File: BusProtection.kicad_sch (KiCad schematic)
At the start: 90 parts, among them Q1 NX3008NBKS, Q10 MBT2222ADW1T1, Q11 NX3008NBKS, Q12 MBT2222ADW1T1, Q13 NX3008NBKS, Q14 MBT2222ADW1T1, Q15 NX3008NBKS, Q16 MBT2222ADW1T1, Q17 MMBT2907, Q18 MMBT2907, Q19 MMBT2907, Q2 MBT2222ADW1T1, Q3 NX3008NBKS, Q4 MBT2222ADW1T1, Q5 NX3008NBKS, Q6 MBT2222ADW1T1, Q7 NX3008NBKS, Q8 MBT2222ADW1T1, Q9 NX3008NBKS

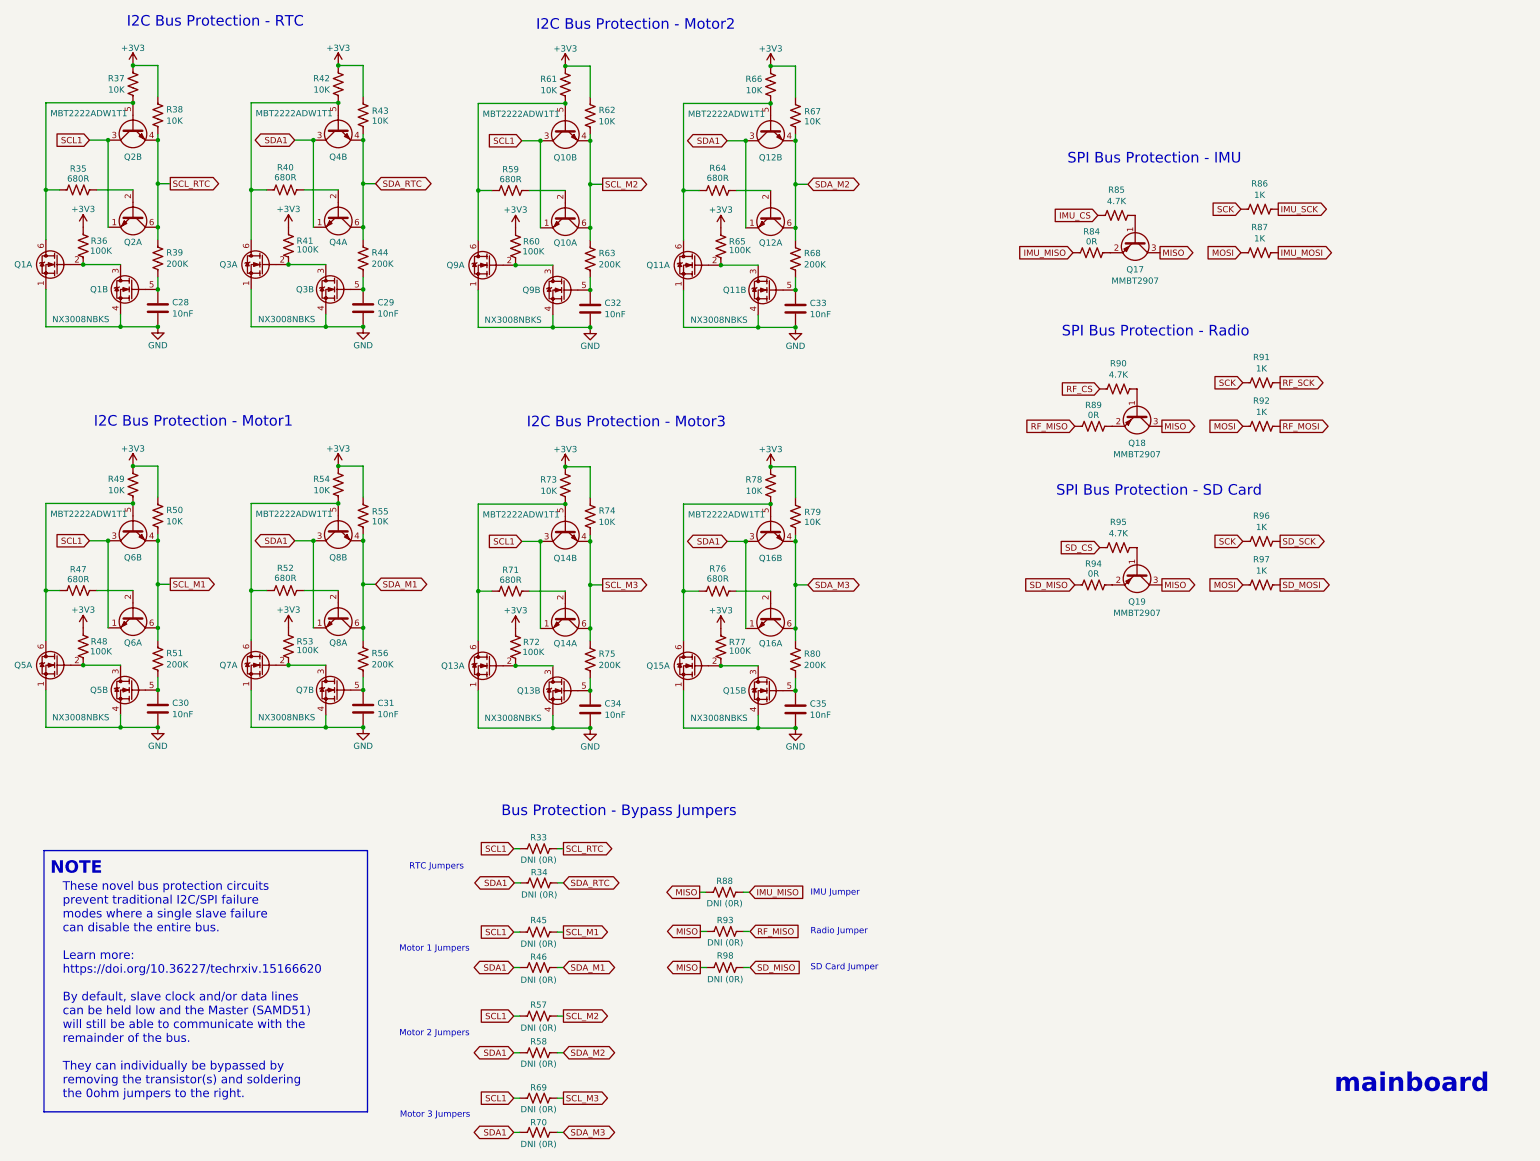
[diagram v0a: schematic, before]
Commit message: Re-wired IMU to use UART
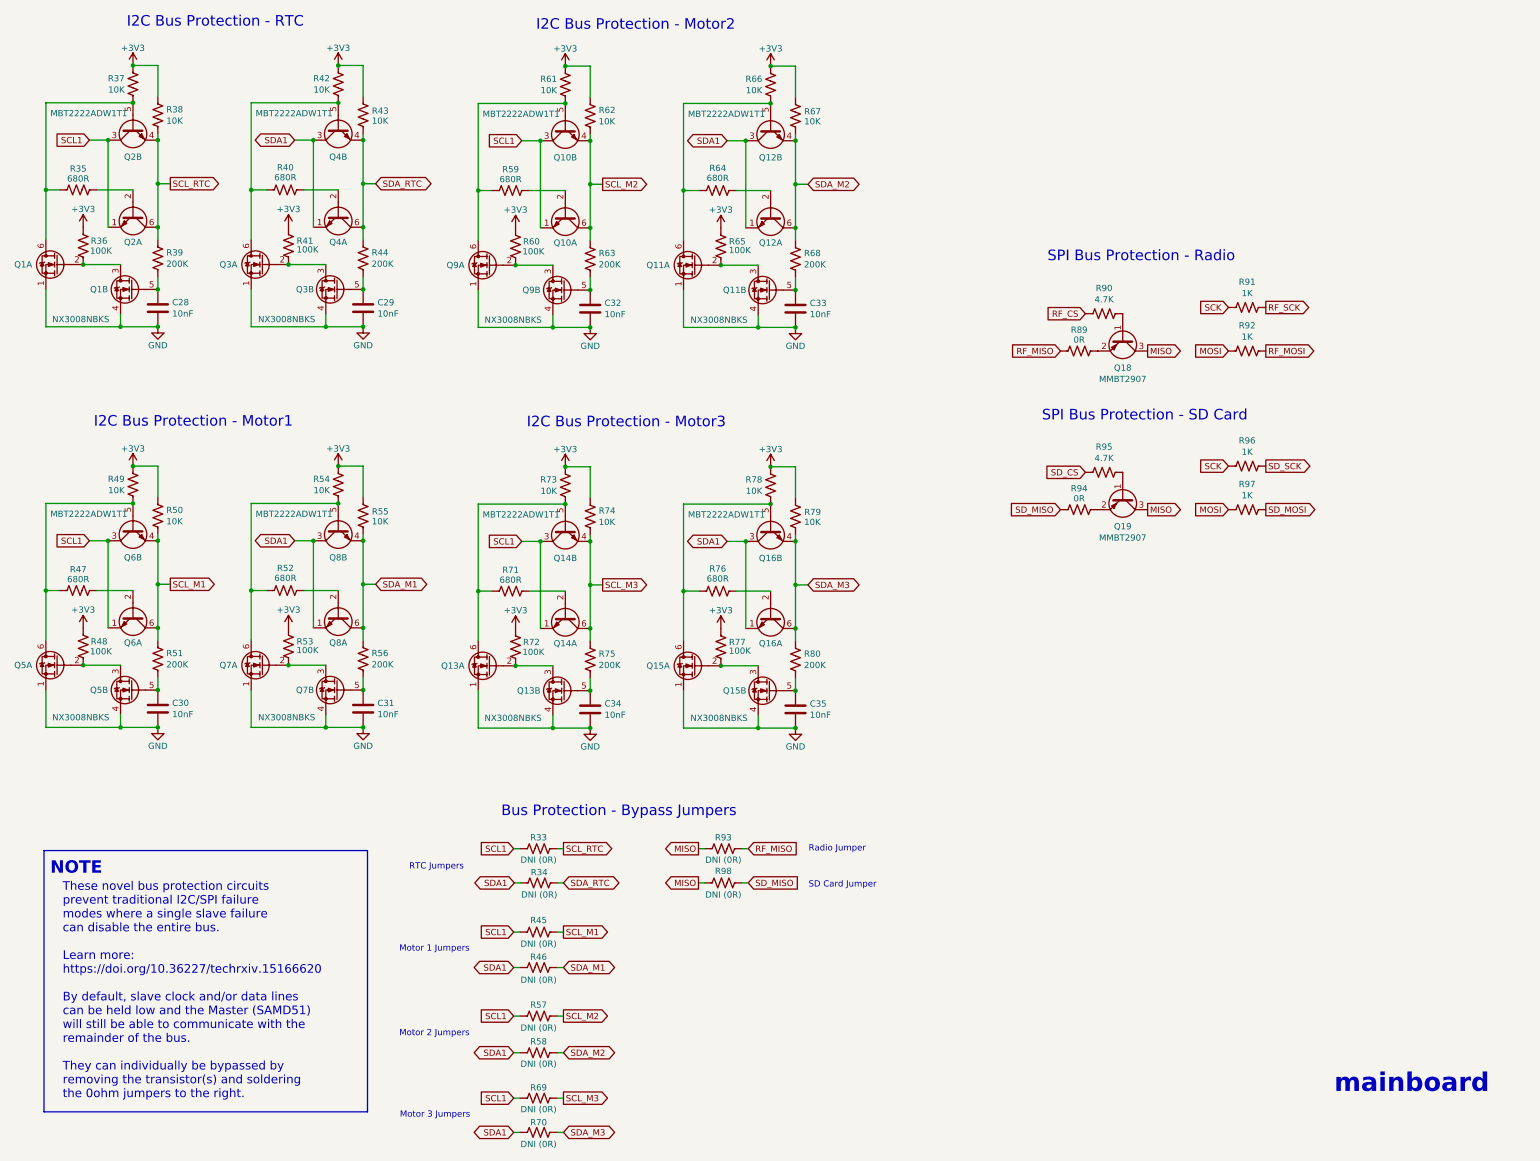
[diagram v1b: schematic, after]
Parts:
- removed Q17: MMBT2907, Package_TO_SOT_SMD:SOT-23, symbol mainboard:MMBT2907
- removed R84: 0R, Resistor_SMD:R_0603_1608Metric, symbol Device:R_US
- removed R85: 4.7K, Resistor_SMD:R_0603_1608Metric, symbol Device:R_US
- removed R86, R87: 1K, Resistor_SMD:R_0603_1608Metric, symbol Device:R_US
- removed R88: DNI (0R), Resistor_SMD:R_0603_1608Metric, symbol Device:R_US
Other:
- note removed: "IMU Jumper"
- note removed: "SPI Bus Protection - IMU"
- moved on the sheet: Q18, Q19, R89, R90, R91, R92, R93, R94, R95, R96, R97, R98

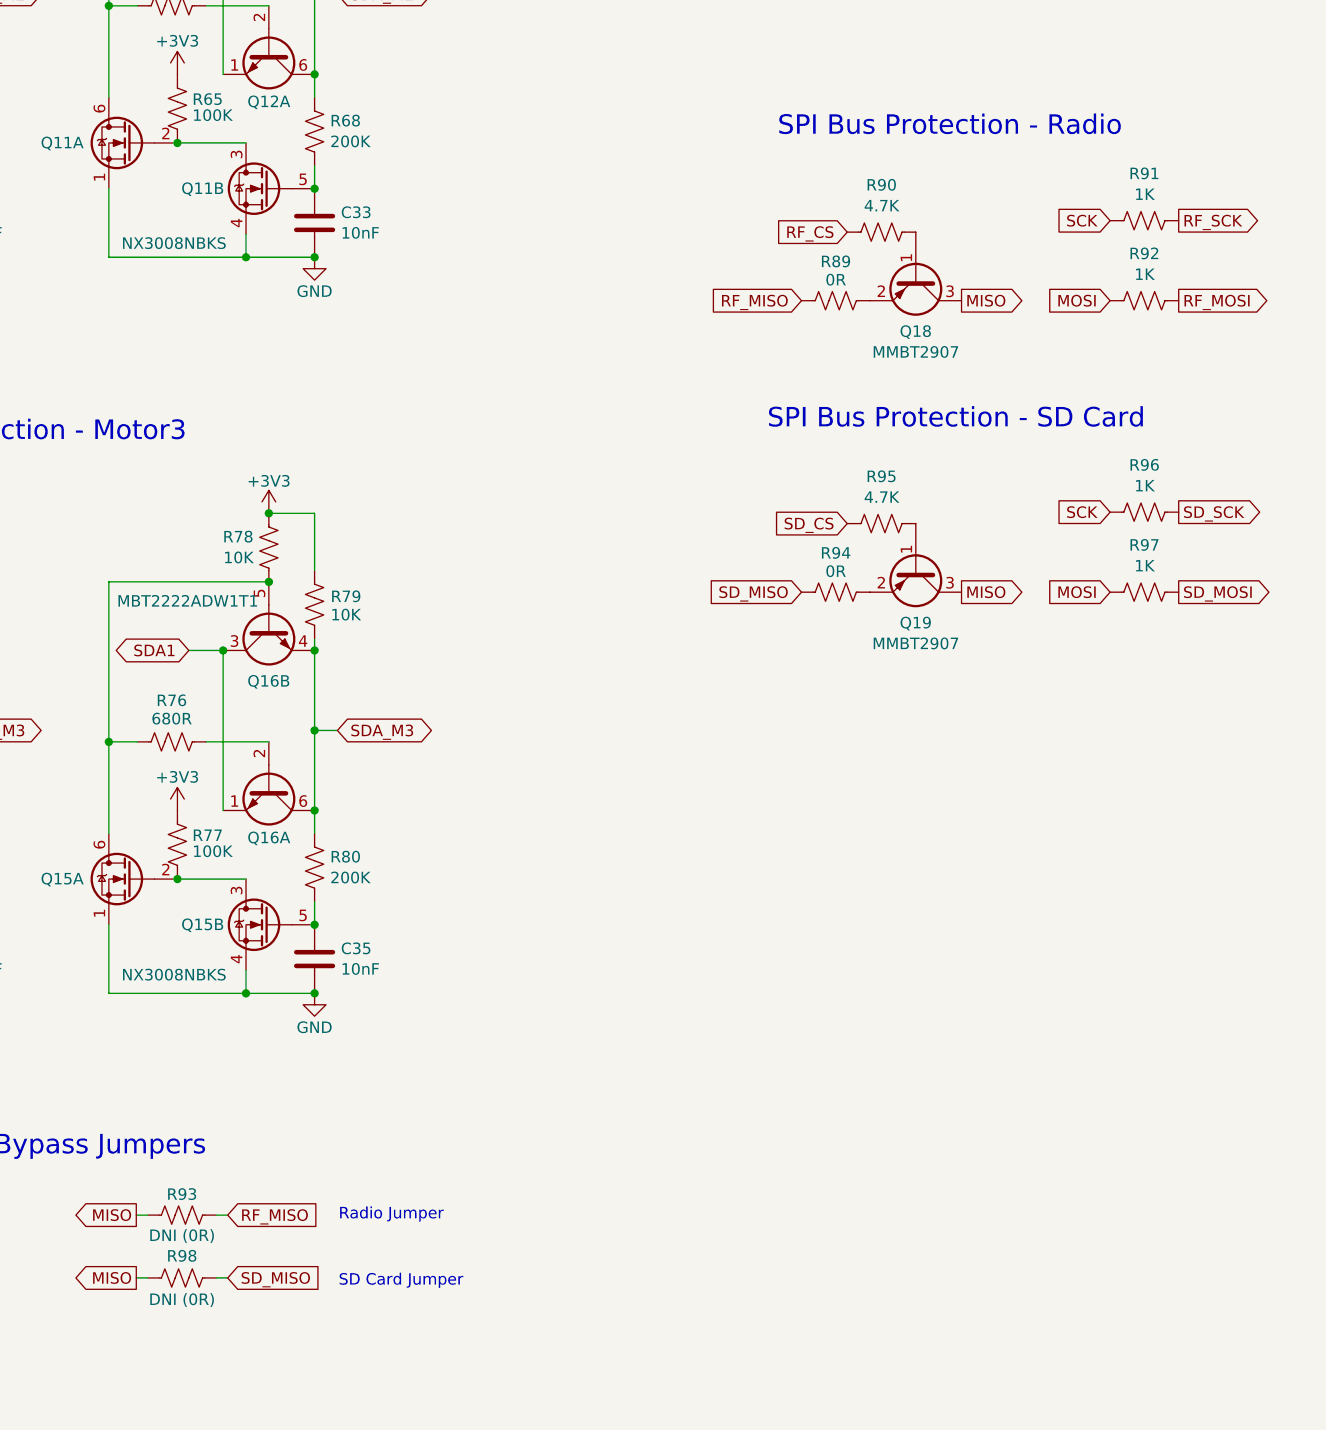
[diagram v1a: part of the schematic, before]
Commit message: Moved Rev label to be visible post-assembly
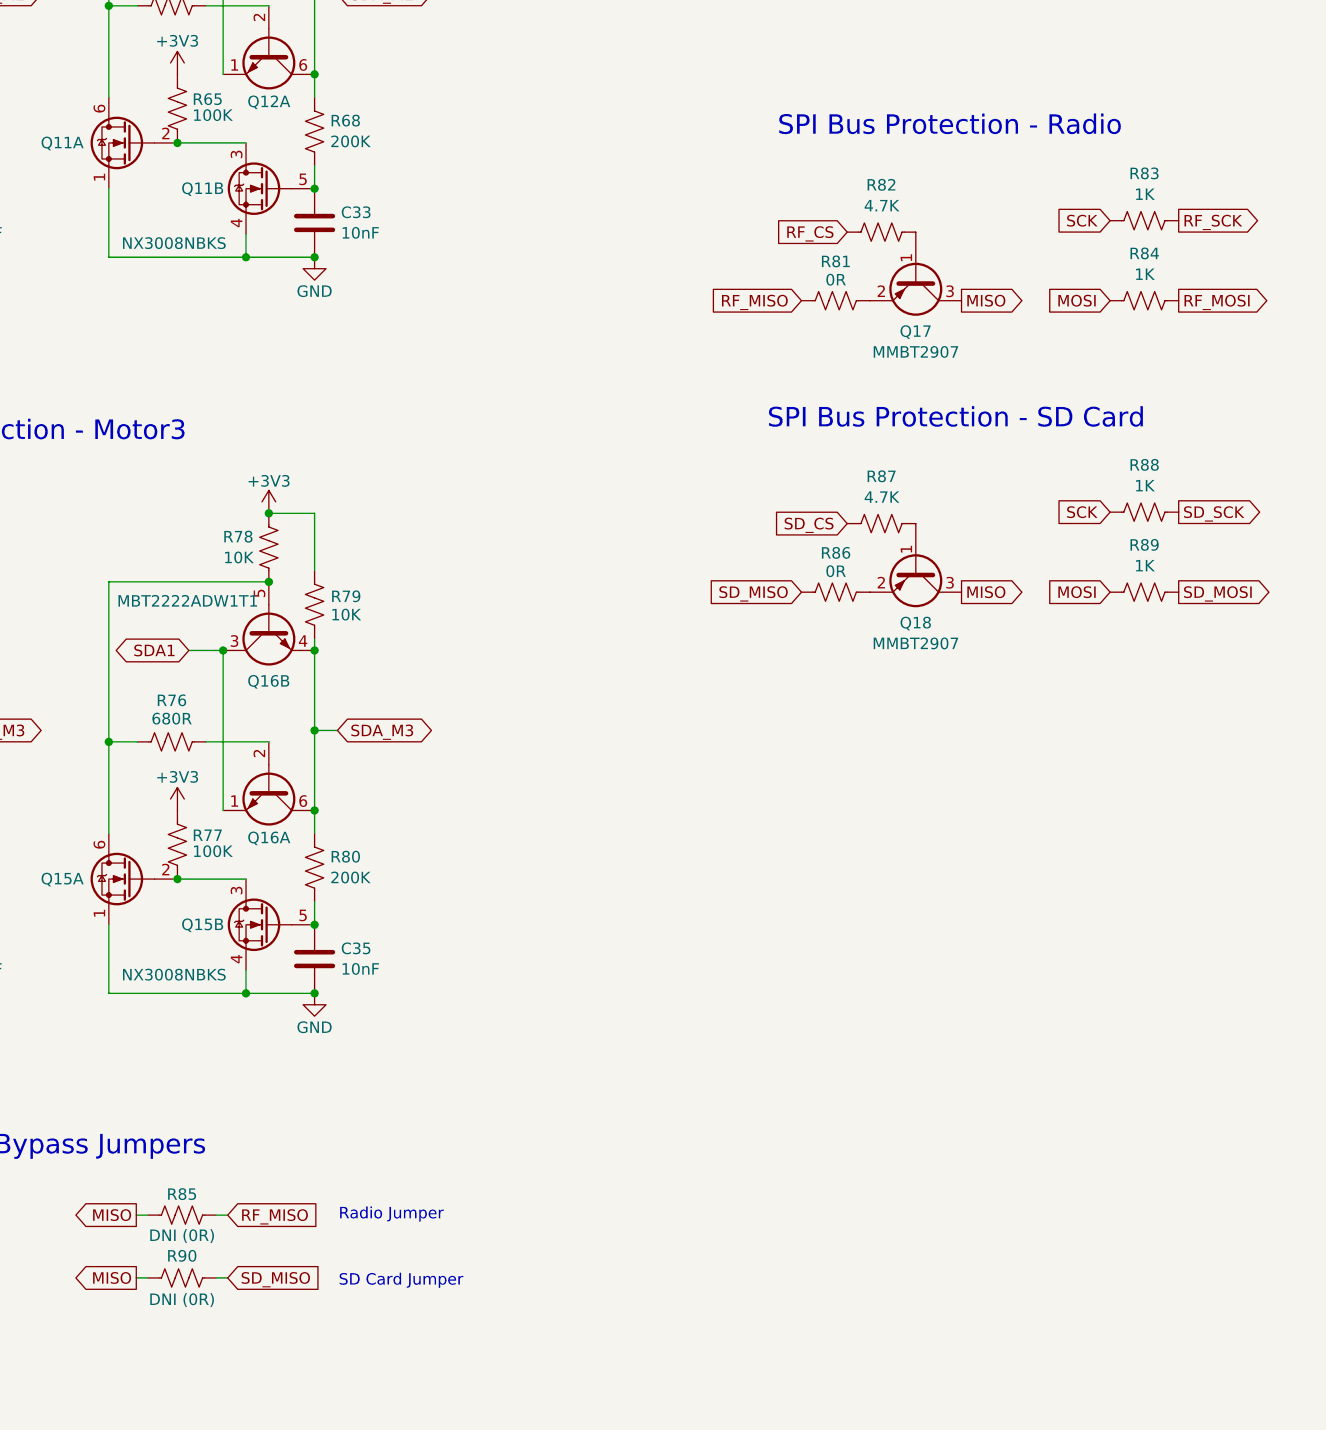
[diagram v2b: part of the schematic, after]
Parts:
- renumbered Q18 to Q17, Q19 to Q18, R89 to R81, R90 to R82, R91 to R83, R92 to R84, R93 to R85, R94 to R86, R95 to R87, R96 to R88, R97 to R89, R98 to R90
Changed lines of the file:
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@@
   (symbol (lib_id "Device:R_US") (at 298.323 126.492 270) (unit 1)
     (in_bom yes) (on_board yes) (dnp no)
-    (property "Reference" "R94" (at 298.323 122.174 90)
+    (property "Reference" "R86" (at 298.323 122.174 90)
       (effects (font (size 1.27 1.27)))
     )
@@
       (project "mainboard"
         (path "/1aa2047c-1463-47dc-8fa9-594d0cbf3c24/89e9ad27-deb2-49f4-bcf8-1a7a63ce9e3a"
-          (reference "R94") (unit 1)
+          (reference "R86") (unit 1)
         )
       )
@@
   (symbol (lib_id "Device:R_US") (at 225.679 202.692 270) (unit 1)
     (in_bom yes) (on_board yes) (dnp no)
-    (property "Reference" "R98" (at 225.679 200.279 90)
+    (property "Reference" "R90" (at 225.679 200.279 90)
       (effects (font (size 1.27 1.27)))
     )
@@
       (project "mainboard"
         (path "/1aa2047c-1463-47dc-8fa9-594d0cbf3c24/89e9ad27-deb2-49f4-bcf8-1a7a63ce9e3a"
-          (reference "R98") (unit 1)
+          (reference "R90") (unit 1)
         )
       )
@@
   (symbol (lib_id "Device:R_US") (at 332.613 94.107 270) (unit 1)
     (in_bom yes) (on_board yes) (dnp no)
-    (property "Reference" "R92" (at 332.613 88.9 90)
+    (property "Reference" "R84" (at 332.613 88.9 90)
       (effects (font (size 1.27 1.27)))
     )
@@
       (project "mainboard"
         (path "/1aa2047c-1463-47dc-8fa9-594d0cbf3c24/89e9ad27-deb2-49f4-bcf8-1a7a63ce9e3a"
-          (reference "R92") (unit 1)
+          (reference "R84") (unit 1)
         )
       )
@@
   (symbol (lib_id "Device:R_US") (at 332.613 126.492 270) (unit 1)
     (in_bom yes) (on_board yes) (dnp no)
-    (property "Reference" "R97" (at 332.613 121.285 90)
+    (property "Reference" "R89" (at 332.613 121.285 90)
       (effects (font (size 1.27 1.27)))
     )
@@
       (project "mainboard"
         (path "/1aa2047c-1463-47dc-8fa9-594d0cbf3c24/89e9ad27-deb2-49f4-bcf8-1a7a63ce9e3a"
-          (reference "R97") (unit 1)
+          (reference "R89") (unit 1)
         )
       )
@@
   (symbol (lib_id "Device:R_US") (at 303.403 118.872 270) (unit 1)
     (in_bom yes) (on_board yes) (dnp no)
-    (property "Reference" "R95" (at 303.403 113.665 90)
+    (property "Reference" "R87" (at 303.403 113.665 90)
       (effects (font (size 1.27 1.27)))
     )
@@
       (project "mainboard"
         (path "/1aa2047c-1463-47dc-8fa9-594d0cbf3c24/89e9ad27-deb2-49f4-bcf8-1a7a63ce9e3a"
-          (reference "R95") (unit 1)
+          (reference "R87") (unit 1)
         )
       )
@@
   (symbol (lib_id "Device:R_US") (at 298.323 94.107 270) (unit 1)
     (in_bom yes) (on_board yes) (dnp no)
-    (property "Reference" "R89" (at 298.323 89.789 90)
+    (property "Reference" "R81" (at 298.323 89.789 90)
       (effects (font (size 1.27 1.27)))
     )
@@
       (project "mainboard"
         (path "/1aa2047c-1463-47dc-8fa9-594d0cbf3c24/89e9ad27-deb2-49f4-bcf8-1a7a63ce9e3a"
-          (reference "R89") (unit 1)
+          (reference "R81") (unit 1)
         )
       )
@@
   (symbol (lib_id "mainboard:MMBT2907") (at 307.213 123.952 270) (unit 1)
     (in_bom yes) (on_board yes) (dnp no)
-    (property "Reference" "Q19" (at 307.213 129.921 90)
+    (property "Reference" "Q18" (at 307.213 129.921 90)
       (effects (font (size 1.27 1.27)))
     )
@@
       (project "mainboard"
         (path "/1aa2047c-1463-47dc-8fa9-594d0cbf3c24/89e9ad27-deb2-49f4-bcf8-1a7a63ce9e3a"
-          (reference "Q19") (unit 1)
+          (reference "Q18") (unit 1)
         )
       )
@@
   (symbol (lib_id "mainboard:MMBT2907") (at 307.213 91.567 270) (unit 1)
     (in_bom yes) (on_board yes) (dnp no)
-    (property "Reference" "Q18" (at 307.213 97.536 90)
+    (property "Reference" "Q17" (at 307.213 97.536 90)
       (effects (font (size 1.27 1.27)))
     )
@@
       (project "mainboard"
         (path "/1aa2047c-1463-47dc-8fa9-594d0cbf3c24/89e9ad27-deb2-49f4-bcf8-1a7a63ce9e3a"
-          (reference "Q18") (unit 1)
+          (reference "Q17") (unit 1)
         )
       )
@@
   (symbol (lib_id "Device:R_US") (at 303.403 86.487 270) (unit 1)
     (in_bom yes) (on_board yes) (dnp no)
-    (property "Reference" "R90" (at 303.403 81.28 90)
+    (property "Reference" "R82" (at 303.403 81.28 90)
       (effects (font (size 1.27 1.27)))
     )
@@
       (project "mainboard"
         (path "/1aa2047c-1463-47dc-8fa9-594d0cbf3c24/89e9ad27-deb2-49f4-bcf8-1a7a63ce9e3a"
-          (reference "R90") (unit 1)
+          (reference "R82") (unit 1)
         )
       )
@@
   (symbol (lib_id "Device:R_US") (at 225.679 195.707 270) (unit 1)
     (in_bom yes) (on_board yes) (dnp no)
-    (property "Reference" "R93" (at 225.679 193.421 90)
+    (property "Reference" "R85" (at 225.679 193.421 90)
       (effects (font (size 1.27 1.27)))
     )
@@
       (project "mainboard"
         (path "/1aa2047c-1463-47dc-8fa9-594d0cbf3c24/89e9ad27-deb2-49f4-bcf8-1a7a63ce9e3a"
-          (reference "R93") (unit 1)
+          (reference "R85") (unit 1)
         )
       )
@@
   (symbol (lib_id "Device:R_US") (at 332.613 117.602 270) (unit 1)
     (in_bom yes) (on_board yes) (dnp no)
-    (property "Reference" "R96" (at 332.613 112.395 90)
+    (property "Reference" "R88" (at 332.613 112.395 90)
       (effects (font (size 1.27 1.27)))
     )
@@
       (project "mainboard"
         (path "/1aa2047c-1463-47dc-8fa9-594d0cbf3c24/89e9ad27-deb2-49f4-bcf8-1a7a63ce9e3a"
-          (reference "R96") (unit 1)
+          (reference "R88") (unit 1)
         )
       )
@@
   (symbol (lib_id "Device:R_US") (at 332.613 85.217 270) (unit 1)
     (in_bom yes) (on_board yes) (dnp no)
-    (property "Reference" "R91" (at 332.613 80.01 90)
+    (property "Reference" "R83" (at 332.613 80.01 90)
       (effects (font (size 1.27 1.27)))
     )
@@
       (project "mainboard"
         (path "/1aa2047c-1463-47dc-8fa9-594d0cbf3c24/89e9ad27-deb2-49f4-bcf8-1a7a63ce9e3a"
-          (reference "R91") (unit 1)
+          (reference "R83") (unit 1)
         )
       )

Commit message: Stash C1 Updates
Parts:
- removed Q17: MMBT2907, Package_TO_SOT_SMD:SOT-23, symbol mainboard:MMBT2907
- removed R81: 0R, Resistor_SMD:R_0603_1608Metric, symbol Device:R_US
- removed R82: 4.7K, Resistor_SMD:R_0603_1608Metric, symbol Device:R_US
- removed R83, R84: 1K, Resistor_SMD:R_0603_1608Metric, symbol Device:R_US
- removed R85: DNI (0R), Resistor_SMD:R_0603_1608Metric, symbol Device:R_US
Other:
- note removed: "Radio Jumper"
- note removed: "SPI Bus Protection - Radio"
- moved on the sheet: C28, C29, C30, C31, C32, C33, C34, C35, Q10A, Q10B, Q11A, Q11B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
